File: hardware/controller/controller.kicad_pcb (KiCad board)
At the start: 4 copper layers, 59 x 47 mm, 62 parts, among them J1 Conn_01x02_Pin, J11 Barrel_Jack, J12 USB_C_Receptacle_USB2.0_14P, J2 Conn_01x02_Pin, J3 Conn_01x02_Pin, J5 Screw_Terminal_01x02, J6 Screw_Terminal_01x02, J7 Conn_01x04_Pin, J8 Conn_01x04_Pin, U1 ESP32-C3-MINI-1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

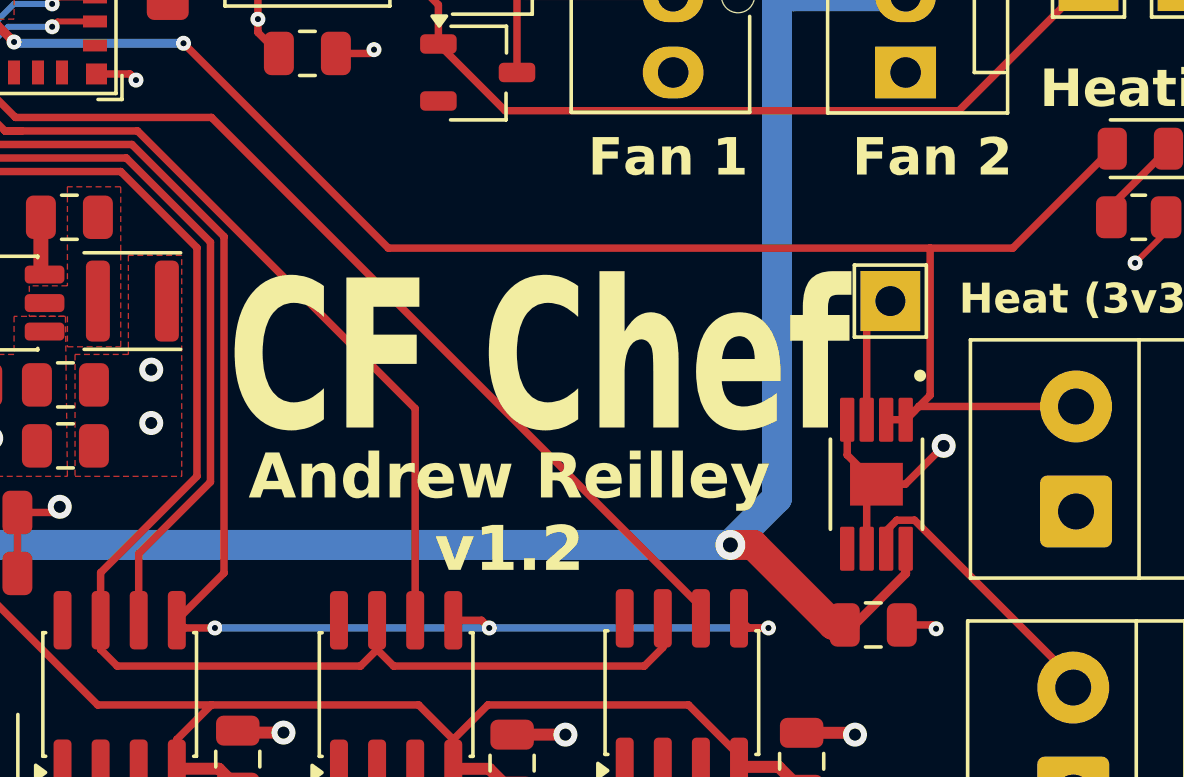
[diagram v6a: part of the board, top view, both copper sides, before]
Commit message: Increase capacitance of MAX caps
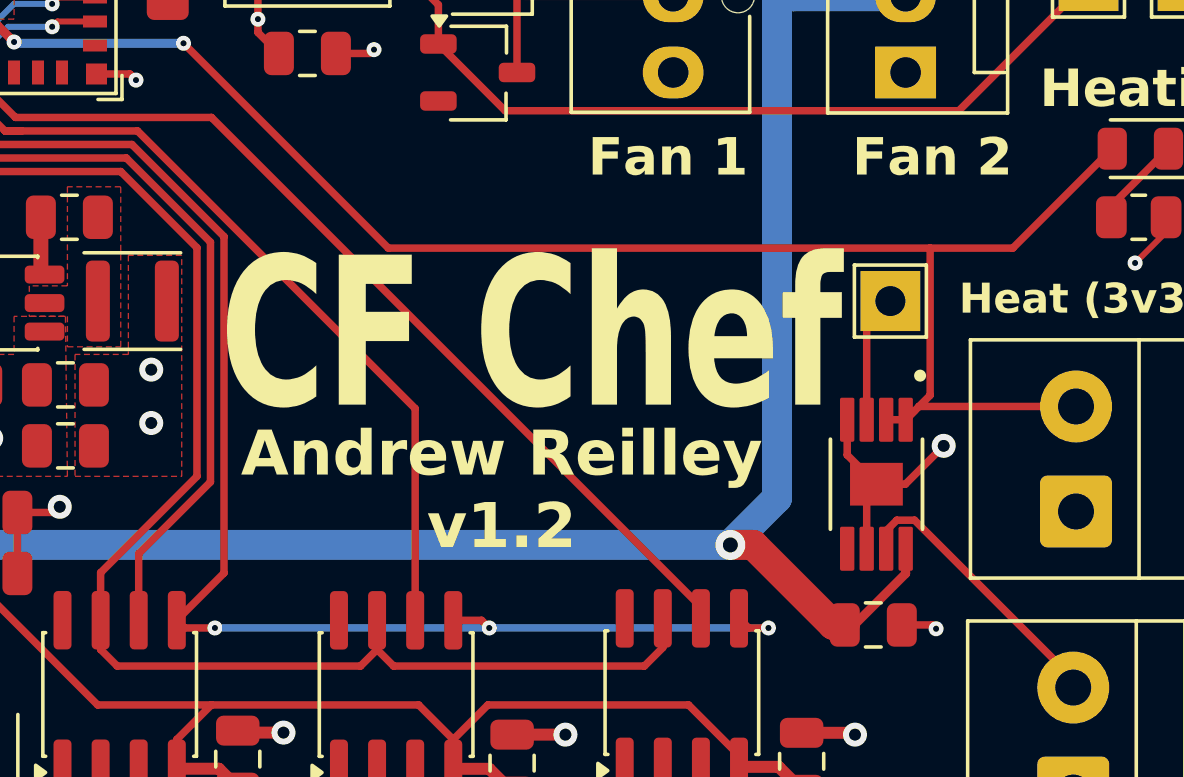
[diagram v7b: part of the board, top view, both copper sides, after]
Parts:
- C3, C4, C6: value 1uF -> 10uF
